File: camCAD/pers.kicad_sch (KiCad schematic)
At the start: 15 parts, among them J1 ILI9341_Display_Header, J2 SWD Header, U1 STM32F407ZGT6 LQFP144

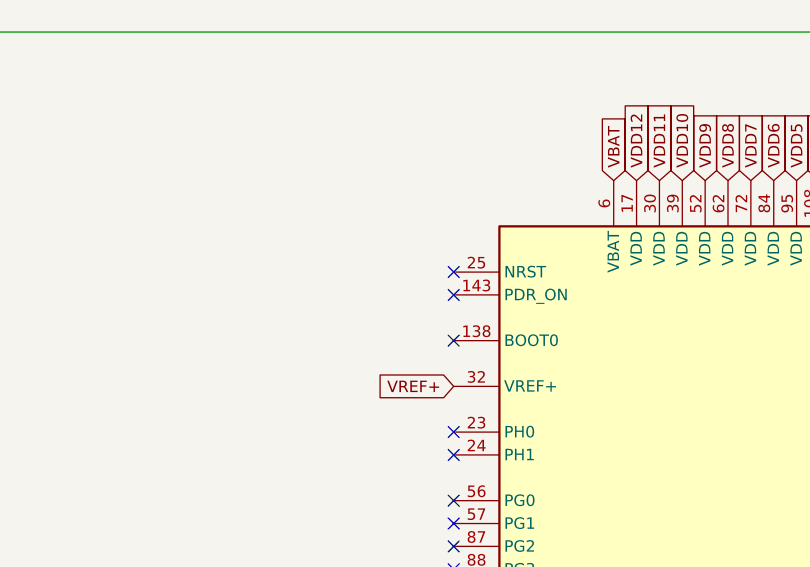
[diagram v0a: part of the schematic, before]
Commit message: Included buck converter schematic
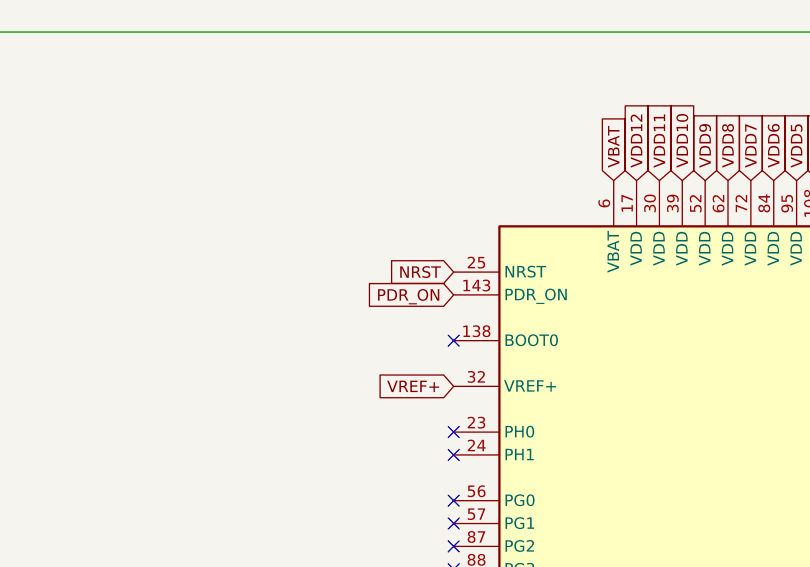
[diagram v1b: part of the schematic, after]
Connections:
- net PDR_ON: now reaches U1.143 (PDR_ON)
- net NRST: now reaches U1.25 (NRST)
- no-connect marks 88 -> 86
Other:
- title: (none) -> Connections to peripherals for camera + storage interface
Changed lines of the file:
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@@
 	(generator_version "10.0")
 	(paper "User" 330.2 381)
+	(title_block
+		(title "Connections to peripherals for camera + storage interface")
+		(date "2026-06-09")
+		(rev "Jun26")
+		(comment 4 "By Siddharth Vasudevan")
+	)
 	(text "SWDIO"
 		(exclude_from_sim no)
@@
 	(no_connect
 		(at 196.85 214.63)
-	)
-	(no_connect
-		(at 130.81 80.01)
-	)
-	(no_connect
-		(at 130.81 77.47)
 	)
 	(no_connect
@@
 			)
 		)
+	)
+	(global_label "PDR_ON"
+		(shape input)
+		(at 130.81 80.01 180)
+		(fields_autoplaced yes)
+		(effects
+			(font
+				(size 1.27 1.27)
+			)
+			(justify right)
+		)
+		(property "Intersheetrefs" "${INTERSHEET_REFS}"
+			(at 120.3862 80.01 0)
+			(hide yes)
+			(show_name no)
+			(do_not_autoplace no)
+			(effects
+				(font
+					(size 1.27 1.27)
+				)
+				(justify right)
+			)
+		)
+	)
+	(global_label "NRST"
+		(shape input)
+		(at 130.81 77.47 180)
+		(fields_autoplaced yes)
+		(effects
+			(font
+				(size 1.27 1.27)
+			)
+			(justify right)
+		)
+		(property "Intersheetrefs" "${INTERSHEET_REFS}"
+			(at 123.0472 77.47 0)
+			(hide yes)
+			(show_name no)
+			(do_not_autoplace no)
+			(effects
+				(font
+					(size 1.27 1.27)
+				)
+				(justify right)
+			)
+		)
